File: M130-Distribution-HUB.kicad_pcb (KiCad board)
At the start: 4 copper layers, 152.4 x 114.3 mm, 20 parts, among them CN0 6437288-3

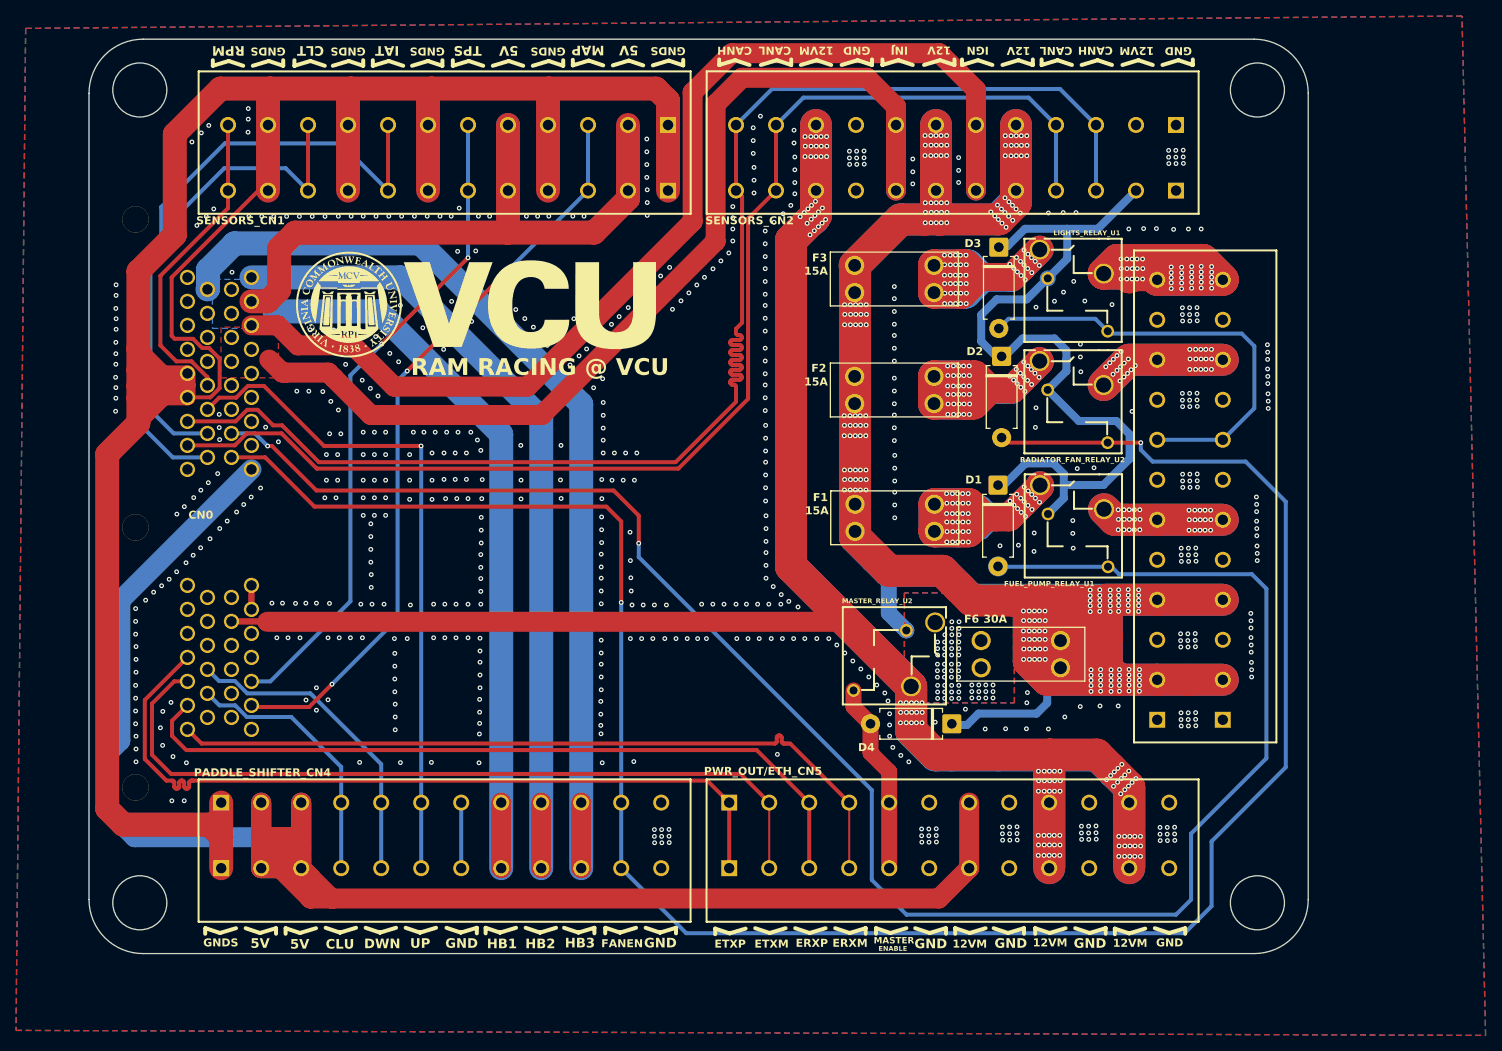
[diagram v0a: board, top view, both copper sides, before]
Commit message: Engine GND bolt
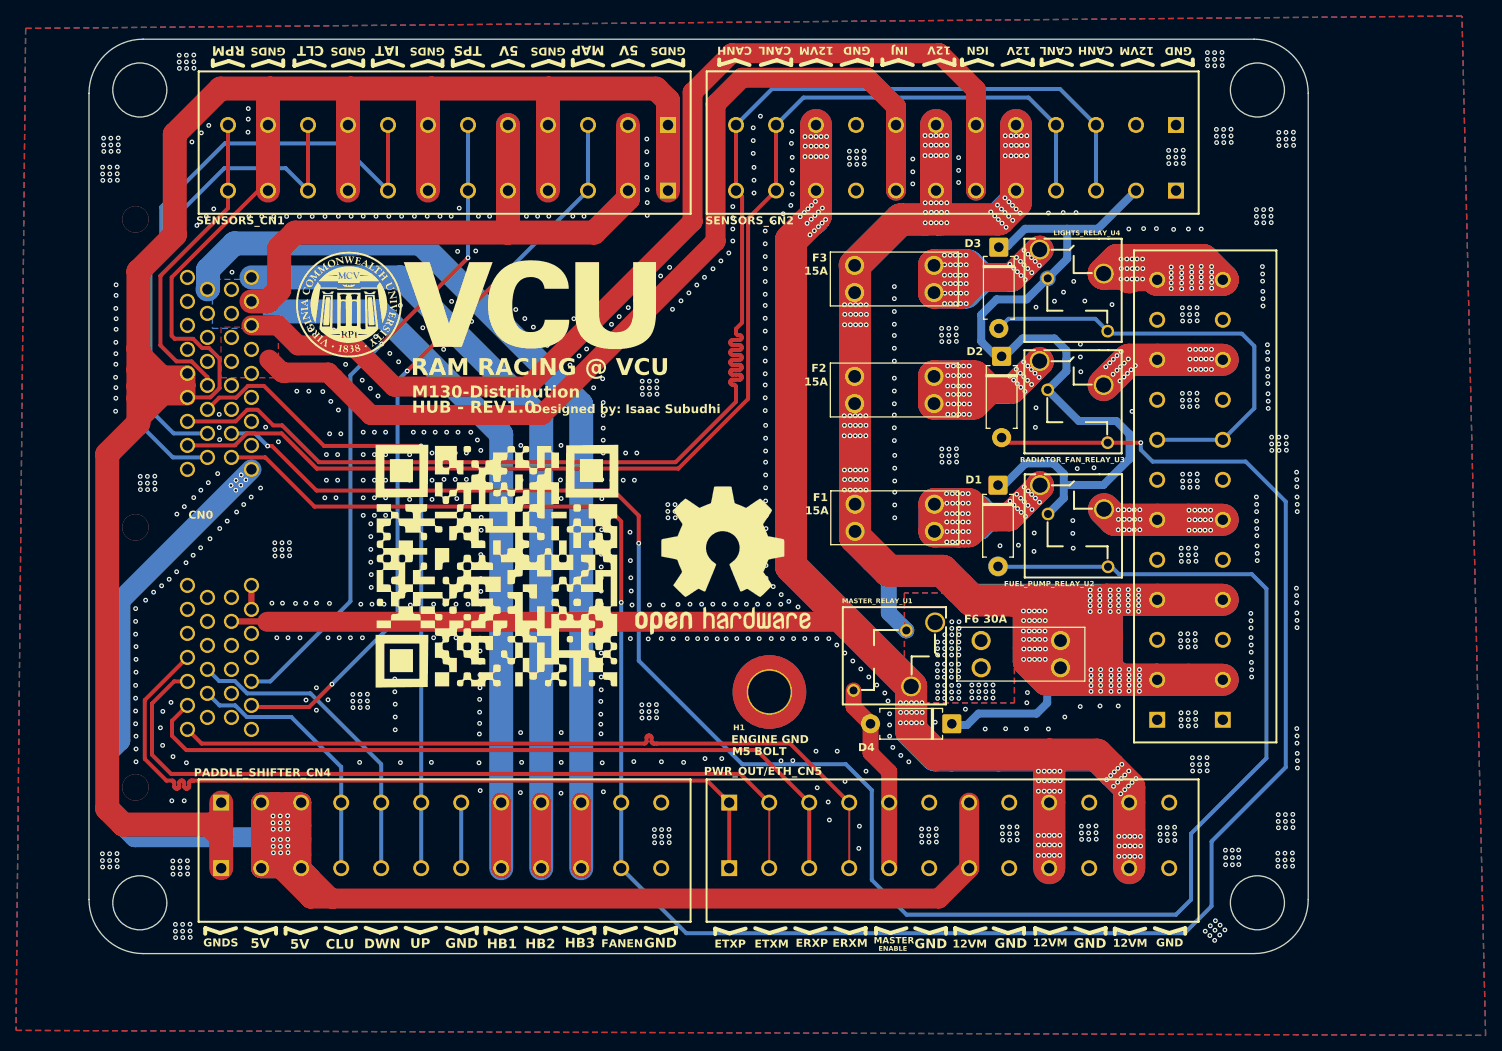
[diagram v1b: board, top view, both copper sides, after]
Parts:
- added G***: LOGO, LOGO, F.Cu at (111.5, 104.3)
- added H1: MountingHole_Pad, MountingHole:MountingHole_5.3mm_M5_DIN965_Pad_TopBottom, F.Cu at (145.4, 120.1)
- added REF**: OSHW-Logo2_24.3x20mm_SilkScreen, Symbol:OSHW-Logo2_24.3x20mm_SilkScreen, F.Cu at (139.6, 103.6)
- F3: value 15A -> 10A
- moved REF** 55.2 mm to (131.1, 67.0)
- renumbered FUEL_PUMP_RELAY_U1 to FUEL_PUMP_RELAY_U2, LIGHTS_RELAY_U1 to LIGHTS_RELAY_U4, MASTER_RELAY_U2 to MASTER_RELAY_U1, RADIATOR_FAN_RELAY_U2 to RADIATOR_FAN_RELAY_U3
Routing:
- net /A09-SEN_5V0_B: track 245.9 -> 279.3 mm
- net /A23-INJ_LS1: track 233.0 -> 240.6 mm
- net GND: vias 624 -> 912
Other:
- board text added: "Designed on Earth"
- board text added: "ENGINE GND"
- board text added: "M5 BOLT"
